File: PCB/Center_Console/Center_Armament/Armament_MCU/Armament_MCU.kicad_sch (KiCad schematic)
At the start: 0 parts

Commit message: Armament_MCU schematic prep: docs, library symbols, root sheet
- Center_Armament.md: correct J2 pinout, GPIO allocation, power
  architecture, remove wrong gate pull-up and NPN driver rows
- hardware-standards.md: clarify 12V+5V bus / local AMS1117-3.3
  architecture; AP63205WU only for future high-current boards
- kicad.md: mark IRLML2502, DRV8835 Ready; SN65HVD230 → built-in
- OpenSkyhawk.kicad_sym: add IRLML2502 (SOT-23 N-MOSFET) and
  DRV8835 (HTSSOP-16 dual H-bridge) symbols
- Armament_MCU.kicad_sch: add 4 hierarchical sub-sheet references
  (MCU_CAN, Switches, Backlighting, Gauges)
- Armament_MCU.kicad_pro: update project settings
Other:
- added sheet Backlighting (Backlighting.kicad_sch)
- added sheet Gauges (Gauges.kicad_sch)
- added sheet MCU_CAN (MCU_CAN.kicad_sch)
- added sheet Switches (Switches.kicad_sch)
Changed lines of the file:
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@@
 (kicad_sch
-  (version 20260306)
-  (generator "eeschema")
-  (generator_version "10.0")
-  (paper "A4")
-  (title_block
-    (title "Armament_MCU")
-    (date "2026-05-17")
-    (rev "1.0")
-    (company "OpenSkyhawk")
-  )
-  (sheet_instances
-    (path "/"
-      (page "1")
-    )
-  )
+	(version 20260306)
+	(generator "eeschema")
+	(generator_version "10.0")
+	(paper "A4")
+	(title_block
+		(title "Armament_MCU")
+		(date "2026-05-17")
+		(rev "1.0")
+		(company "OpenSkyhawk")
+	)
+	(sheet
+		(at 59.69 57.15)
+		(size 48.26 41.91)
+		(exclude_from_sim no)
+		(in_bom yes)
+		(on_board yes)
+		(dnp no)
+		(fields_autoplaced yes)
+		(stroke
+			(width 0.1524)
+			(type solid)
+		)
+		(fill
+			(color 0 0 0 0)
+		)
+		(property "Sheetname" "MCU_CAN"
+			(at 59.69 56.4384 0)
+			(show_name no)
+			(do_not_autoplace no)
+			(effects
+				(font
+					(size 1.27 1.27)
+				)
+				(justify left bottom)
+			)
+		)
+		(property "Sheetfile" "MCU_CAN.kicad_sch"
+			(at 59.69 99.6446 0)
+			(show_name no)
+			(do_not_autoplace no)
+			(effects
+				(font
+					(size 1.27 1.27)
+				)
+				(justify left top)
+			)
+		)
+		(instances
+			(project "Armament_MCU"
+				(path "/00e506c2-6e76-43a3-96c1-24869bd3aa84"
+					(page "2")
+				)
+			)
+		)
+	)
+	(sheet
+		(at 59.055 125.095)
+		(size 51.435 41.275)
+		(exclude_from_sim no)
+		(in_bom yes)
+		(on_board yes)
+		(dnp no)
+		(fields_autoplaced yes)
+		(stroke
+			(width 0.1524)
+			(type solid)
+		)
+		(fill
+			(color 0 0 0 0)
+		)
+		(property "Sheetname" "Backlighting"
+			(at 59.055 124.3834 0)
+			(show_name no)
+			(do_not_autoplace no)
+			(effects
+				(font
+					(size 1.27 1.27)
+				)
+				(justify left bottom)
+			)
+		)
+		(property "Sheetfile" "Backlighting.kicad_sch"
+			(at 59.055 166.9546 0)
+			(show_name no)
+			(do_not_autoplace no)
+			(effects
+				(font
+					(size 1.27 1.27)
+				)
+				(justify left top)
+			)
+		)
+		(instances
+			(project "Armament_MCU"
+				(path "/00e506c2-6e76-43a3-96c1-24869bd3aa84"
+					(page "4")
+				)
+			)
+		)
+	)
+	(sheet
+		(at 128.905 127.635)
+		(size 42.545 40.005)
+		(exclude_from_sim no)
+		(in_bom yes)
+		(on_board yes)
+		(dnp no)
+		(fields_autoplaced yes)
+		(stroke
+			(width 0.1524)
+			(type solid)
+		)
+		(fill
+			(color 0 0 0 0)
+		)
+		(property "Sheetname" "Gauges"
+			(at 128.905 126.9234 0)
+			(show_name no)
+			(do_not_autoplace no)
+			(effects
+				(font
+					(size 1.27 1.27)
+				)
+				(justify left bottom)
+			)
+		)
+		(property "Sheetfile" "Gauges.kicad_sch"
+			(at 128.905 168.2246 0)
+			(show_name no)
+			(do_not_autoplace no)
+			(effects
+				(font
+					(size 1.27 1.27)
+				)
+				(justify left top)
+			)
+		)
+		(instances
+			(project "Armament_MCU"
+				(path "/00e506c2-6e76-43a3-96c1-24869bd3aa84"
+					(page "5")
+				)
+			)
+		)
+	)
+	(sheet
+		(at 126.365 57.15)
+		(size 43.815 43.18)
+		(exclude_from_sim no)
+		(in_bom yes)
+		(on_board no)
+		(dnp no)
+		(fields_autoplaced yes)
+		(stroke
+			(width 0.1524)
+			(type solid)
+		)
+		(fill
+			(color 0 0 0 0)
+		)
+		(property "Sheetname" "Switches"
+			(at 126.365 56.4384 0)
+			(show_name no)
+			(do_not_autoplace no)
+			(effects
+				(font
+					(size 1.27 1.27)
+				)
+				(justify left bottom)
+			)
+		)
+		(property "Sheetfile" "Switches.kicad_sch"
+			(at 126.365 100.9146 0)
+			(show_name no)
+			(do_not_autoplace no)
+			(effects
+				(font
+					(size 1.27 1.27)
+				)
+				(justify left top)
+			)
+		)
+		(instances
+			(project "Armament_MCU"
+				(path "/00e506c2-6e76-43a3-96c1-24869bd3aa84"
+					(page "3")
+				)
+			)
+		)
+	)
+	(sheet_instances
+		(path "/"
+			(page "1")
+		)
+	)
+	(embedded_fonts no)
 )

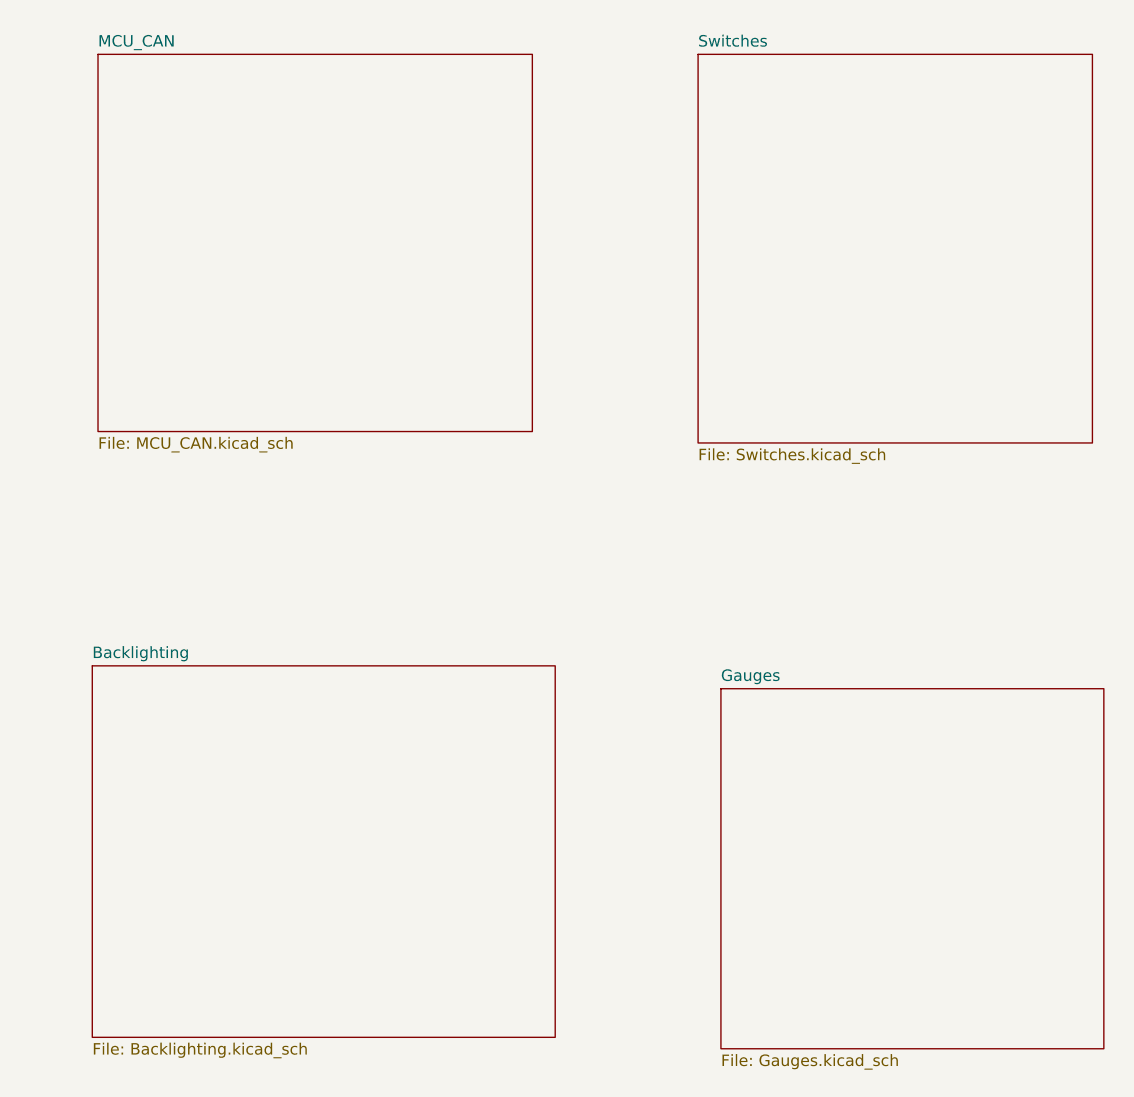
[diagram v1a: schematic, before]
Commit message: Add Armament_MCU 4-sheet hierarchical schematic (first complete revision)
MCU_CAN sheet: STM32F103CBT6 (LQFP48), AMS1117-3.3 (SOT-223), SN65HVD230
CAN transceiver (SOIC-8), 8 MHz HSE crystal (PD0/PD1), two Molex Mini-Fit Jr
2×4 main bus connectors (J_BUS_IN/OUT), SWD + UART debug headers, I2C pull-ups
and series dampers for J_MISC and J_AWRS harnesses, MISSILE_VOL ADC RC filter
(PA2), stepper control labels (PB8–PB12), PWM labels (PA6/PA7), DNP 120Ω CAN
termination footprint.

Backlighting sheet: two IRLML2502 N-ch low-side MOSFET zones — Zone 1 (panel,
4 LED strings × 5 LEDs + 4 generic AUX Mini-Fit Jr outputs), Zone 2 (cabin
pressure gauge, 1 string × 5 LEDs). 100Ω gate series, 100kΩ gate pull-down per
zone.

Gauges sheet: DRV8833PW placeholder for DRV8835 (pending library rework),
X27.589 Switec stepper (MOT1), VM/VCC decoupling. MODE→GND and PGND wiring
deferred until DRV8835 symbol is fixed.

Switches sheet: empty placeholder — Armament Panel direct switch inputs deferred.

Root sheet wires all 4 sub-sheets; all hierarchical labels matched; ERC clean
across all sheets.

Also updates hardware-standards.md (power architecture, main bus pinout) and
Center_Armament.md (definitive J2 harness pinout, I2C addresses, pin
assignments).
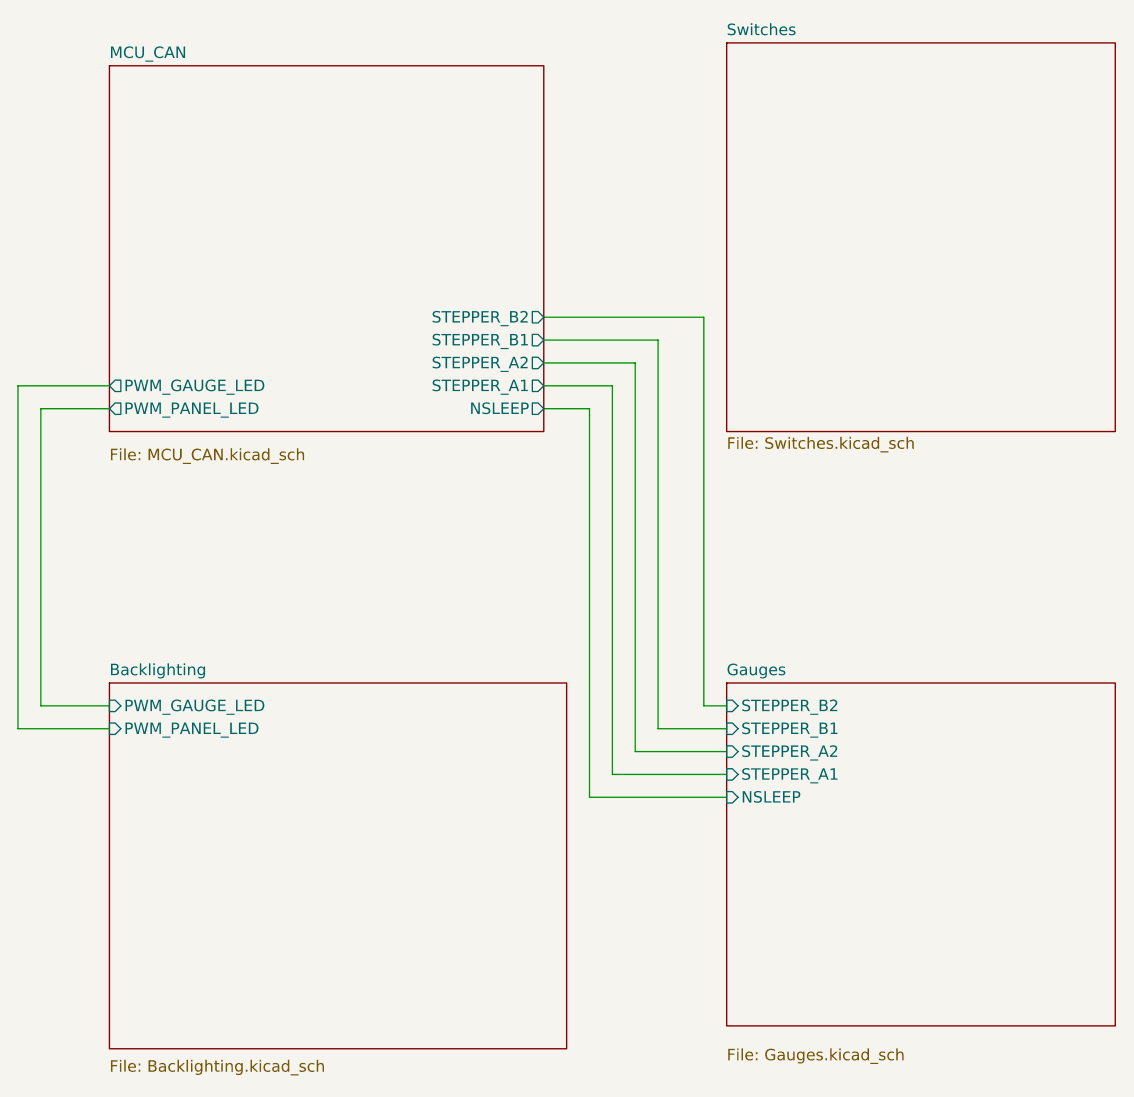
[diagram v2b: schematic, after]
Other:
- sheet Backlighting ports: added PWM_GAUGE_LED, PWM_PANEL_LED; removed none
- sheet Gauges ports: added NSLEEP, STEPPER_A1, STEPPER_A2, STEPPER_B1, STEPPER_B2; removed none
- sheet MCU_CAN ports: added NSLEEP, PWM_GAUGE_LED, PWM_PANEL_LED, STEPPER_A1, STEPPER_A2, STEPPER_B1, STEPPER_B2; removed none
